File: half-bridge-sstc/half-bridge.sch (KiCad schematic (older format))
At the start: 75 parts, among them J1 Current Transformer, J10 Conn_01x01, J11 Conn_01x01, J2 AC Input 18-24 V, J3 Barrel_Jack, J4 Gate Drive Transformer, J5 Reactive Power Meter, J6 External Disable Optocoupler, J7 Conn_01x01, J8 Feedback Antenna, J9 Conn_01x01, U1 tc4420, U2 tc4420, U3 LM7815_TO220, U4 LM339, U6 40106, U7 4N28

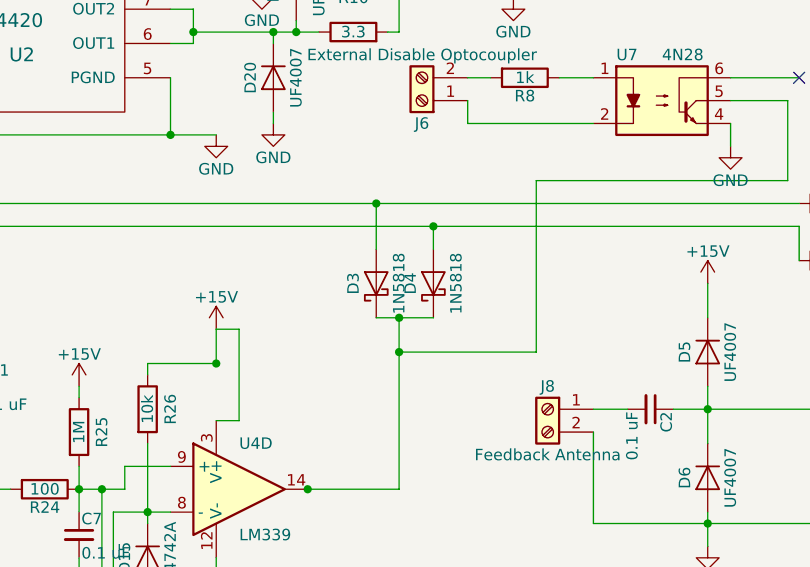
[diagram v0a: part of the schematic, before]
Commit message: Fixed long dead time problem on half-bridge-sstc
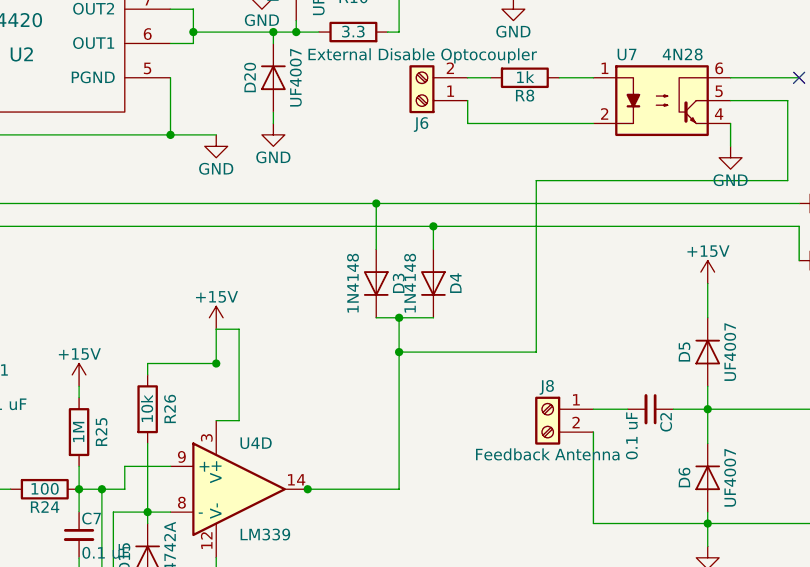
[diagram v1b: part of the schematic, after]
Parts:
- removed D3, D4: 1N5818, Diodes_THT:D_DO-41_SOD81_P7.62mm_Horizontal, symbol D_Schottky
- added D3, D4: 1N4148, Diodes_THT:D_DO-41_SOD81_P7.62mm_Horizontal, symbol D
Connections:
- net at U4.14, U7.5: now also D3.1 (K), D4.1 (K)
- net at R5.1, U2.2 (IN): now also D3.2 (A)
- net at R11.1, U1.2 (IN): now also D4.2 (A)
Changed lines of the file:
@@
-$EndComp
-$Comp
-L D_Schottky D3
-U 1 1 5A7CDC47
-P 6550 3700
-F 0 "D3" H 6550 3800 50  0000 C CNN
-F 1 "1N5818" H 6550 3600 50  0000 C CNN
-F 2 "Diodes_THT:D_DO-41_SOD81_P7.62mm_Horizontal" H 6550 3700 50  0001 C CNN
-F 3 "" H 6550 3700 50  0001 C CNN
-	1    6550 3700
-	0    -1   -1   0
-$EndComp
-$Comp
-L D_Schottky D4
-U 1 1 5A7CDF1D
-P 6800 3700
-F 0 "D4" H 6800 3800 50  0000 C CNN
-F 1 "1N5818" H 6800 3600 50  0000 C CNN
-F 2 "Diodes_THT:D_DO-41_SOD81_P7.62mm_Horizontal" H 6800 3700 50  0001 C CNN
-F 3 "" H 6800 3700 50  0001 C CNN
-	1    6800 3700
-	0    -1   -1   0
 $EndComp
 $Comp
@@
 	9000 2000 9000 3650
 Connection ~ 8950 2000
+$Comp
+L D D3
+U 1 1 5C9D842E
+P 6550 3700
+F 0 "D3" H 6550 3800 50  0000 C CNN
+F 1 "1N4148" H 6550 3600 50  0000 C CNN
+F 2 "Diodes_THT:D_DO-41_SOD81_P7.62mm_Horizontal" H 6550 3700 50  0001 C CNN
+F 3 "" H 6550 3700 50  0001 C CNN
+	1    6550 3700
+	0    1    -1   0
+$EndComp
+$Comp
+L D D4
+U 1 1 5C9D869E
+P 6800 3700
+F 0 "D4" H 6800 3800 50  0000 C CNN
+F 1 "1N4148" H 6800 3600 50  0000 C CNN
+F 2 "Diodes_THT:D_DO-41_SOD81_P7.62mm_Horizontal" H 6800 3700 50  0001 C CNN
+F 3 "" H 6800 3700 50  0001 C CNN
+	1    6800 3700
+	0    1    -1   0
+$EndComp
 $EndSCHEMATC

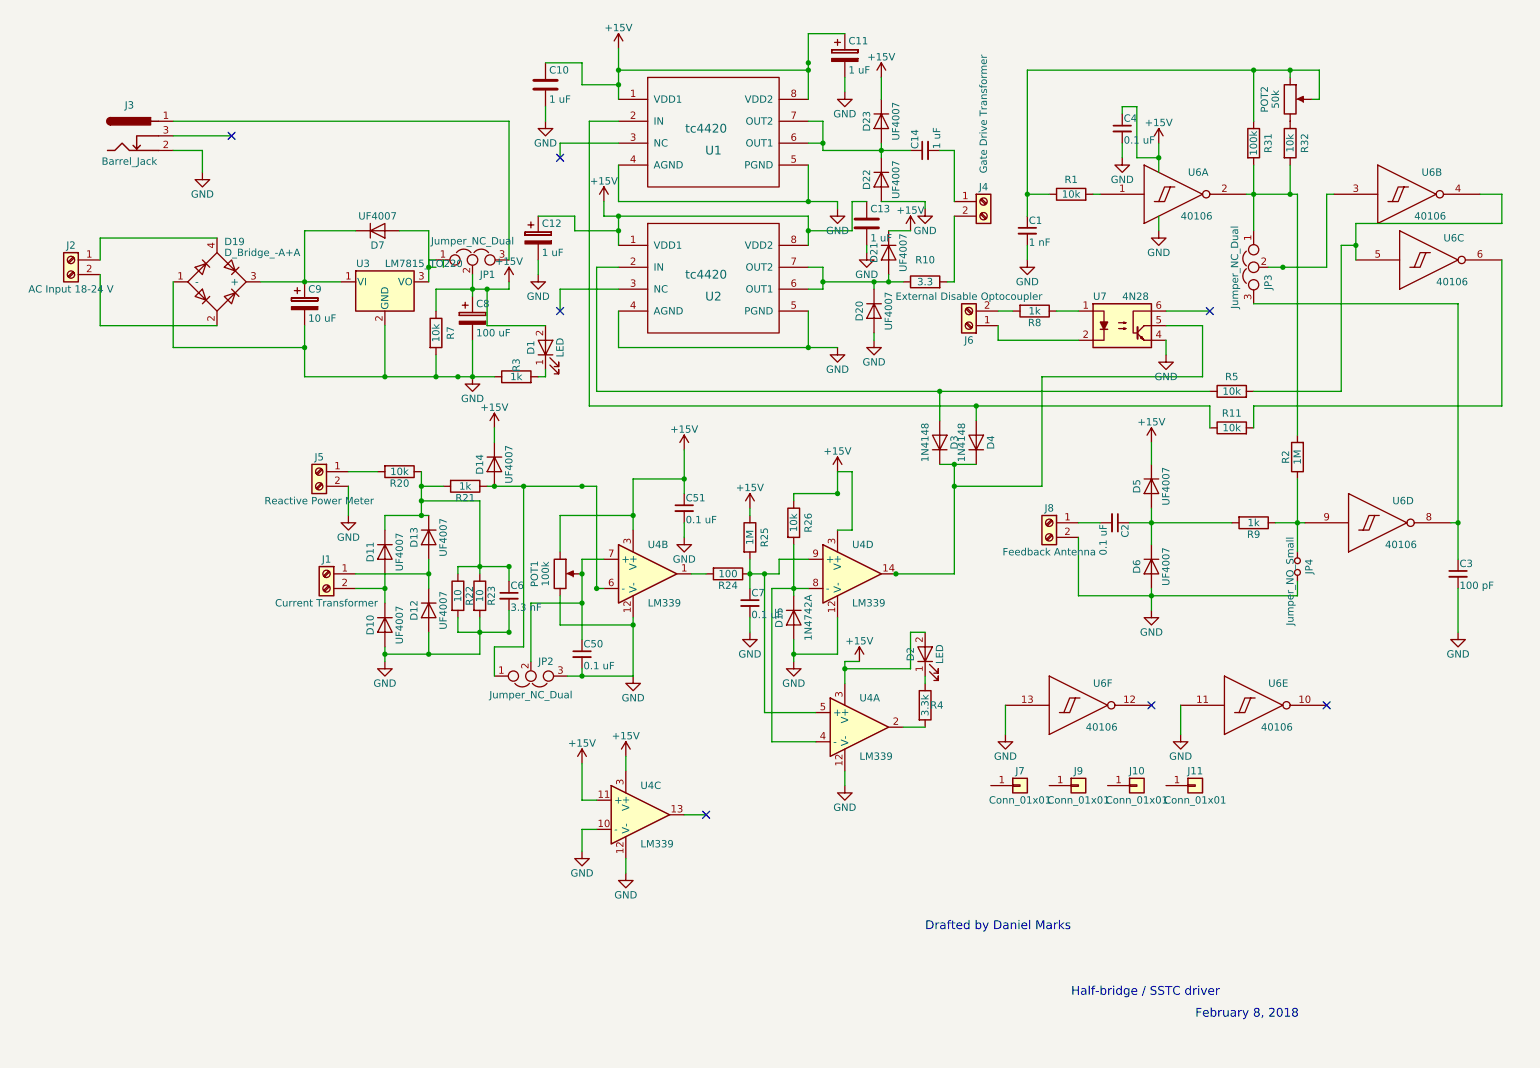
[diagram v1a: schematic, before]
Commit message: Added optional frequency halving to ensure 50% duty cycle
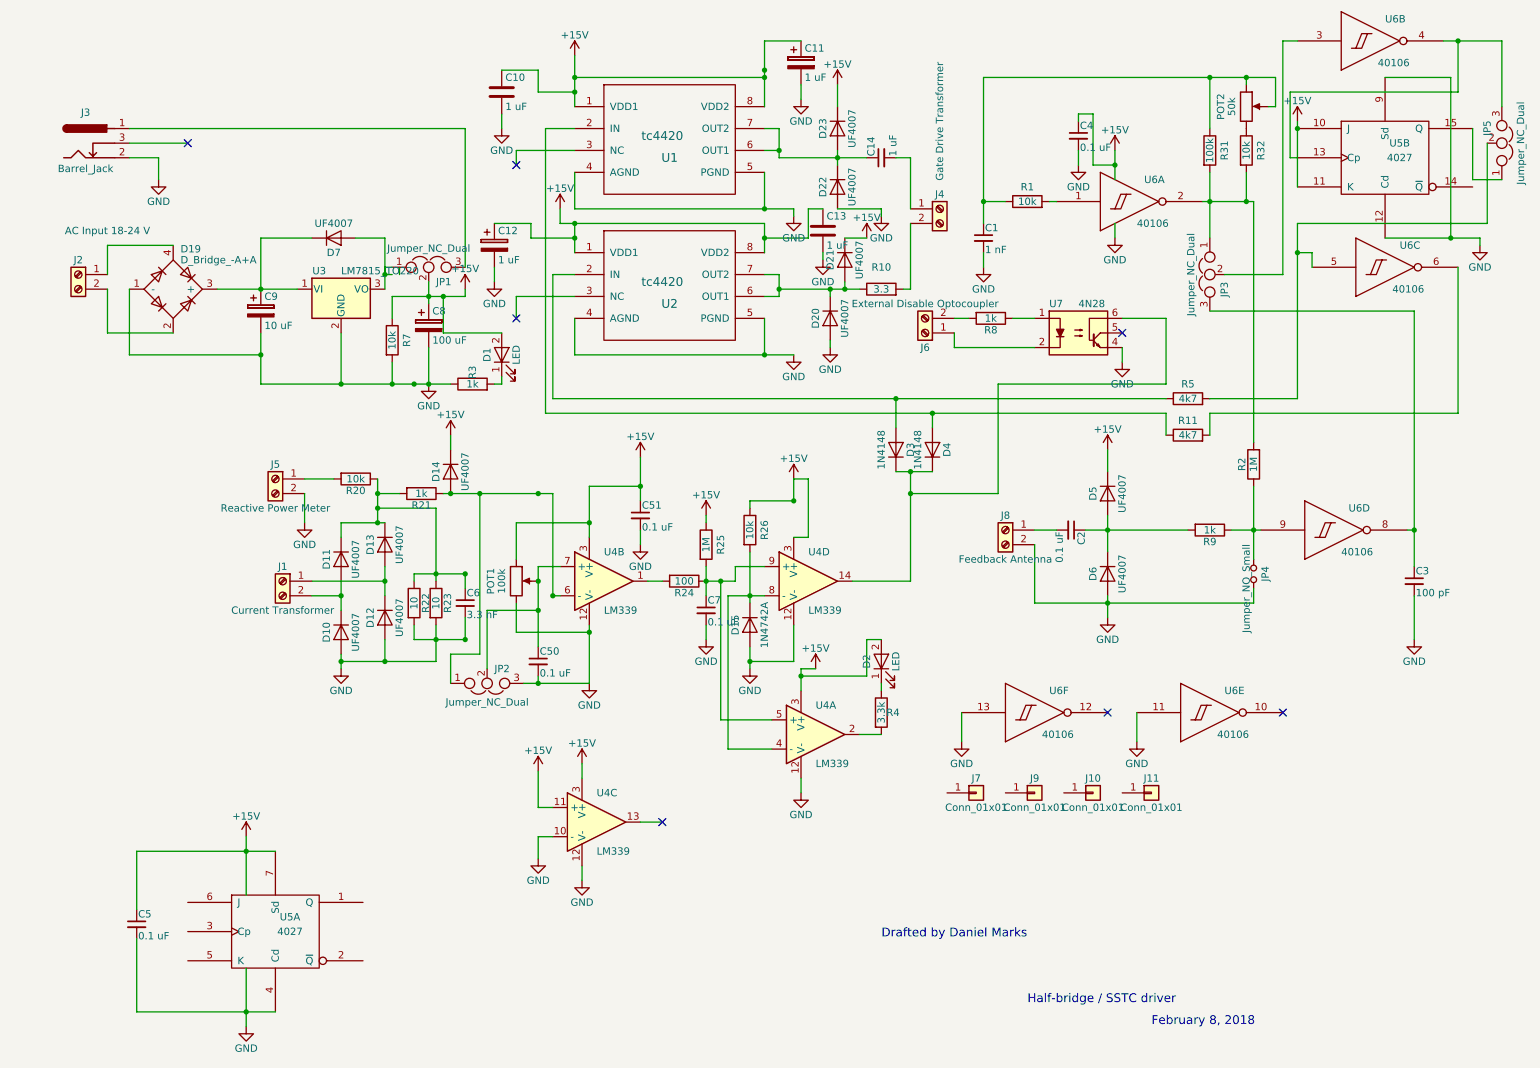
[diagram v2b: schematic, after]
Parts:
- added C5: 0.1 uF, Capacitors_THT:C_Disc_D7.5mm_W4.4mm_P5.00mm, symbol C_Small
- added JP5: Jumper_NC_Dual, Pin_Headers:Pin_Header_Straight_1x03_Pitch2.54mm, symbol Jumper_NC_Dual
- added U5: 4027, Housings_DIP:DIP-16_W7.62mm_Socket, symbol 4027
- R11, R5: value 10k -> 4k7
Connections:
- net +15V: now also C5.1, U5.10 (J), U5.11 (K), U5.16 (VDD), U5.16 (VDD), U5.7 (Sd)
- net GND: now also C5.2, U5.12 (Cd), U5.4 (Cd), U5.8 (VSS), U5.8 (VSS), U5.9 (Sd)
- net at D3.1 (K), D4.1 (K), U4.14: now also U7.6; no longer U7.5
- net at R5.2, U6.5 (In): now also JP5.2; no longer U6.4 (Out)
- new net: JP5.3, U5.13 (Cp), U6.4 (Out)
- new net: JP5.1, U5.15 (Q)
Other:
- moved on the sheet: C1, C10, C11, C12, C13, C14, C2, C3, C4, C50, C51, C6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
